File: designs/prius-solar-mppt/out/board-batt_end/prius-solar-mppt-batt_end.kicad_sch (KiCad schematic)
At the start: 0 parts

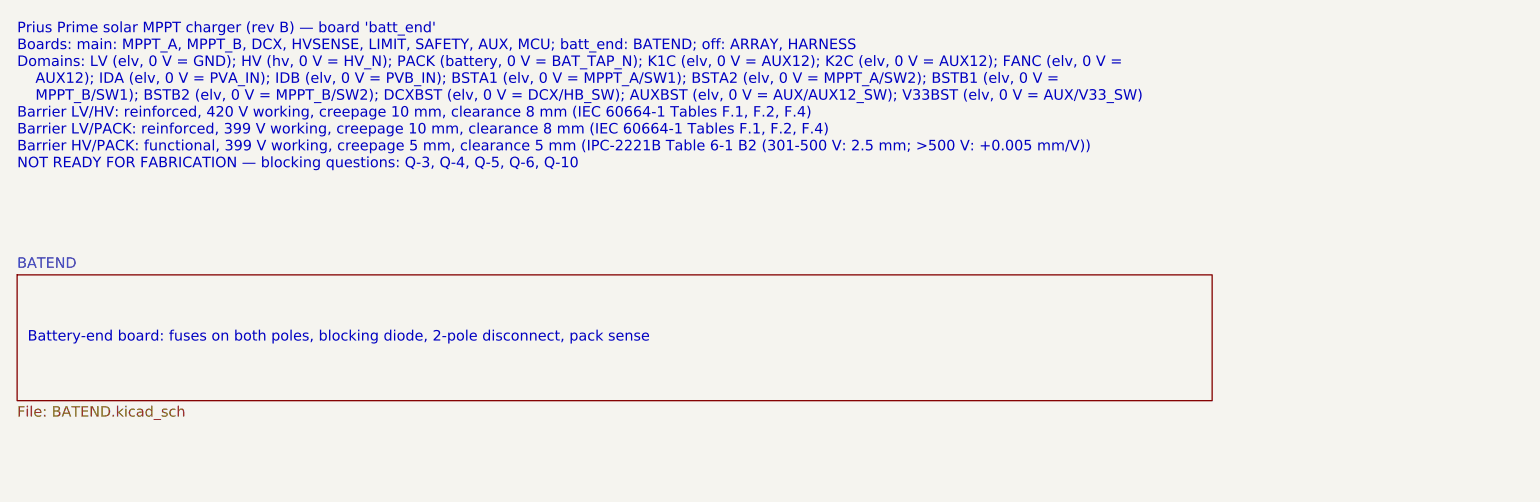
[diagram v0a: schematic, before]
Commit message: designs/prius-solar-mppt: v0.3, fix the independent review's blockers and majors
- B1: CHASSIS domain with reinforced DC barriers to HV and PACK (10/8 mm), HV/PACK edge
  clearance 10 mm, mounting holes fixed with 13 mm keep-outs; thermal pedestal under LV
  parts only.
- B2: no primary source for the Prime's full-charge cell voltage was found (blocking
  Q-13); hardware clamp set below a 4.00 V/cell floor (L3 3.927 V, worst 3.963 V; L2
  3.836 V; L1 3.79 V) with DNP trim to raise later; until then charging may stop near
  55-65 % SOC.
- Majors: sink clamp + burst disable + PV-node trip and TVS against LM5176 reverse power;
  20 MHz AEC-Q200 crystal for CAN (listen-only start); parked insulation monitoring via a
  110 M bridge (also detects a welded relay); open-sensor-safe hardware OT; CAGE CLAMP HV
  terminals with a lid-switch HVIL; DCX on-time and 17.6 A primary overcurrent latches;
  supercap-held latch that clears overnight.
- Build: 0 errors, ERC clean, system and both board netlists identical; 9 waivers (17
  findings, was 32).

Co-Authored-By: Claude Opus 5.5 <noreply@anthropic.com>
Claude-Session: https://claude.ai/code/session_01VFJn9VbX8h27kf4LpLwEtn
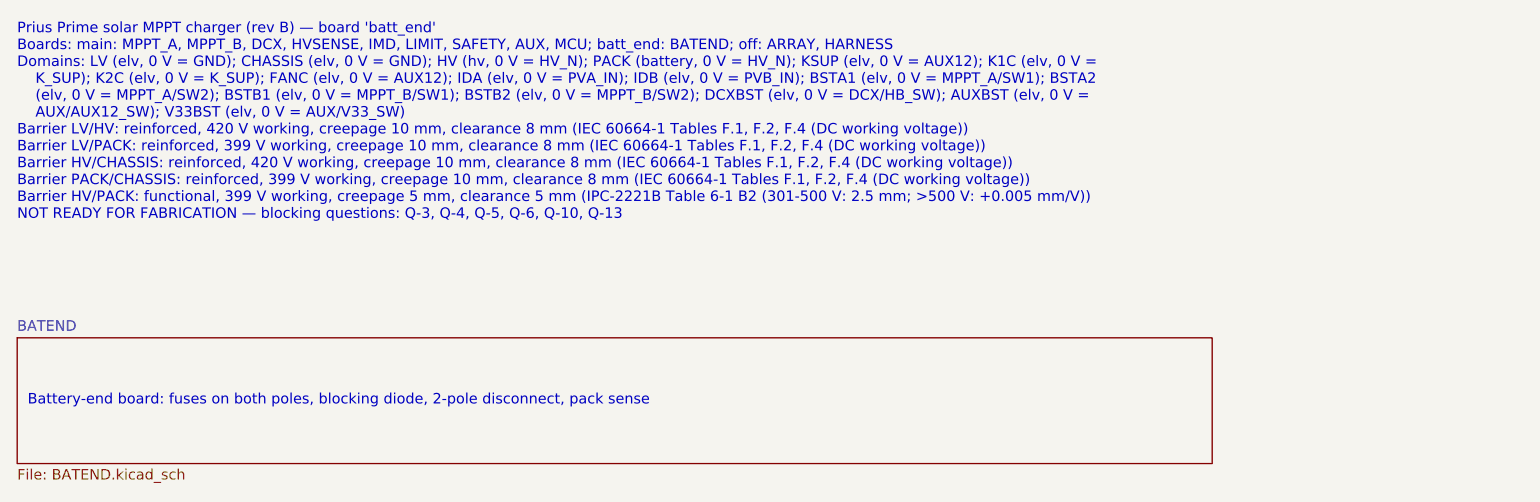
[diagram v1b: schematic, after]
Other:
- note added: "Prius Prime solar MPPT charger (rev B) — board 'batt_end' Boards: main: MPPT_A, MPPT_B, DCX, HVSENSE, IMD, LIMIT, SAFETY, AUX, MCU; batt_end: BATEND; off: ARRAY, HARNESS Domains: LV (elv, 0 V = GND); CHASSIS (elv, 0 V = GND); HV (hv, 0 V = HV_N); PACK (battery, 0 V = HV_N); KSUP (elv, 0 V = AUX12); K1C (elv, 0 V = K_SUP); K2C (elv, 0 V = K_SUP); FANC (elv, 0 V = AUX12); IDA (elv, 0 V = PVA_IN); I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"
- note removed: "Prius Prime solar MPPT charger (rev B) — board 'batt_end' Boards: main: MPPT_A, MPPT_B, DCX, HVSENSE, LIMIT, SAFETY, AUX, MCU; batt_end: BATEND; off: ARRAY, HARNESS Domains: LV (elv, 0 V = GND); HV (hv, 0 V = HV_N); PACK (battery, 0 V = BAT_TAP_N); K1C (elv, 0 V = AUX12); K2C (elv, 0 V = AUX12); FANC (elv, 0 V = AUX12); IDA (elv, 0 V = PVA_IN); IDB (elv, 0 V = PVB_IN); BSTA1 (elv, 0 V = MPPT_A/SW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"
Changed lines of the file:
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@@
 	)
 	(sheet
-		(at 25.4 55.88)
+		(at 25.4 63.5)
 		(size 144.78 15.24)
 		(exclude_from_sim no)
@@
 		)
 		(property "Sheetname" "BATEND"
-			(at 25.4 55.18 0)
+			(at 25.4 62.8 0)
 			(effects
 				(font (size 1.27 1.27))
@@
 		)
 		(property "Sheetfile" "BATEND.kicad_sch"
-			(at 25.4 71.72 0)
+			(at 25.4 79.34 0)
 			(effects
 				(font (size 1.27 1.27))
@@
 	(text "Battery-end board: fuses on both poles, blocking diode, 2-pole disconnect, pack sense"
 		(exclude_from_sim no)
-		(at 26.67 63.5 0)
+		(at 26.67 71.12 0)
 		(effects
 			(font (size 1.27 1.27))
@@
 		)
 	)
-	(text "Prius Prime solar MPPT charger (rev B) — board 'batt_end'\nBoards: main: MPPT_A, MPPT_B, DCX, HVSENSE, LIMIT, SAFETY, AUX, MCU; batt_end: BATEND; off: ARRAY, HARNESS\nDomains: LV (elv, 0 V = GND); HV (hv, 0 V = HV_N); PACK (battery, 0 V = BAT_TAP_N); K1C (elv, 0 V = AUX12); K2C (elv, 0 V = AUX12); FANC (elv, 0 V =\n    AUX12); IDA (elv, 0 V = PVA_IN); IDB (elv, 0 V = PVB_IN); BSTA1 (elv, 0 V = MPPT_A/SW1); BSTA2 (elv, 0 V = MPPT_A/SW2); BSTB1 (elv, 0 V =\n    MPPT_B/SW1); BSTB2 (elv, 0 V = MPPT_B/SW2); DCXBST (elv, 0 V = DCX/HB_SW); AUXBST (elv, 0 V = AUX/AUX12_SW); V33BST (elv, 0 V = AUX/V33_SW)\nBarrier LV/HV: reinforced, 420 V working, creepage 10 mm, clearance 8 mm (IEC 60664-1 Tables F.1, F.2, F.4)\nBarrier LV/PACK: reinforced, 399 V working, creepage 10 mm, clearance 8 mm (IEC 60664-1 Tables F.1, F.2, F.4)\nBarrier HV/PACK: functional, 399 V working, creepage 5 mm, clearance 5 mm (IPC-2221B Table 6-1 B2 (301-500 V: 2.5 mm; >500 V: +0.005 mm/V))\nNOT READY FOR FABRICATION — blocking questions: Q-3, Q-4, Q-5, Q-6, Q-10"
+	(text "Prius Prime solar MPPT charger (rev B) — board 'batt_end'\nBoards: main: MPPT_A, MPPT_B, DCX, HVSENSE, IMD, LIMIT, SAFETY, AUX, MCU; batt_end: BATEND; off: ARRAY, HARNESS\nDomains: LV (elv, 0 V = GND); CHASSIS (elv, 0 V = GND); HV (hv, 0 V = HV_N); PACK (battery, 0 V = HV_N); KSUP (elv, 0 V = AUX12); K1C (elv, 0 V =\n    K_SUP); K2C (elv, 0 V = K_SUP); FANC (elv, 0 V = AUX12); IDA (elv, 0 V = PVA_IN); IDB (elv, 0 V = PVB_IN); BSTA1 (elv, 0 V = MPPT_A/SW1); BSTA2\n    (elv, 0 V = MPPT_A/SW2); BSTB1 (elv, 0 V = MPPT_B/SW1); BSTB2 (elv, 0 V = MPPT_B/SW2); DCXBST (elv, 0 V = DCX/HB_SW); AUXBST (elv, 0 V =\n    AUX/AUX12_SW); V33BST (elv, 0 V = AUX/V33_SW)\nBarrier LV/HV: reinforced, 420 V working, creepage 10 mm, clearance 8 mm (IEC 60664-1 Tables F.1, F.2, F.4 (DC working voltage))\nBarrier LV/PACK: reinforced, 399 V working, creepage 10 mm, clearance 8 mm (IEC 60664-1 Tables F.1, F.2, F.4 (DC working voltage))\nBarrier HV/CHASSIS: reinforced, 420 V working, creepage 10 mm, clearance 8 mm (IEC 60664-1 Tables F.1, F.2, F.4 (DC working voltage))\nBarrier PACK/CHASSIS: reinforced, 399 V working, creepage 10 mm, clearance 8 mm (IEC 60664-1 Tables F.1, F.2, F.4 (DC working voltage))\nBarrier HV/PACK: functional, 399 V working, creepage 5 mm, clearance 5 mm (IPC-2221B Table 6-1 B2 (301-500 V: 2.5 mm; >500 V: +0.005 mm/V))\nNOT READY FOR FABRICATION — blocking questions: Q-3, Q-4, Q-5, Q-6, Q-10, Q-13"
 		(exclude_from_sim no)
 		(at 25.4 25.4 0)
